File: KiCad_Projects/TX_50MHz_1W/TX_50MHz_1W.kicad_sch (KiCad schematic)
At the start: 3 parts, among them Q1 1W PA, U1 ESP32-S3, U2 Si5351A

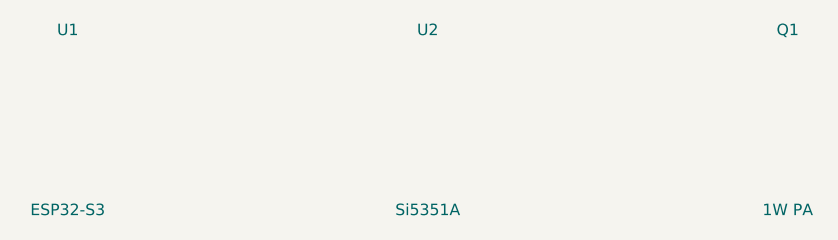
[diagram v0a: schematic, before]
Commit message: Add .kicad_pro project files for better compatibility with KiCad 8.0+
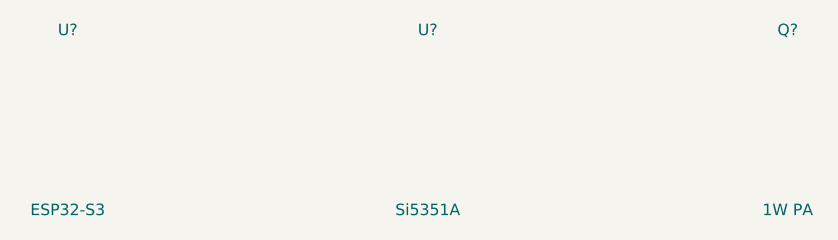
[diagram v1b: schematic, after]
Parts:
- renumbered Q1 to Q?, U1 to U?, U2 to U?
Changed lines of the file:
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@@
-(kicad_sch (version 20211123) (generator eeschema)
-  (paper "A4")
-  (symbol (lib_id "ESP32-S3-WROOM-1") (at 100 100 0) (unit 1)
-    (in_bom yes) (on_board yes) (fields_autoplaced)
-    (property "Reference" "U1" (id 0) (at 100 90 0))
-    (property "Value" "ESP32-S3" (id 1) (at 100 110 0))
-  )
-  (symbol (lib_id "RD01MUS2") (at 180 100 0) (unit 1)
-    (in_bom yes) (on_board yes) (fields_autoplaced)
-    (property "Reference" "Q1" (id 0) (at 180 90 0))
-    (property "Value" "1W PA" (id 1) (at 180 110 0))
-  )
-  (symbol (lib_id "Si5351A") (at 140 100 0) (unit 1)
-    (in_bom yes) (on_board yes) (fields_autoplaced)
-    (property "Reference" "U2" (id 0) (at 140 90 0))
-    (property "Value" "Si5351A" (id 1) (at 140 110 0))
-  )
-  (sheet_instances
-    (path "/" (page "1"))
-  )
+(kicad_sch
+	(version 20250114)
+	(generator "eeschema")
+	(generator_version "9.0")
+	(paper "A4")
+	(symbol
+		(lib_id "ESP32-S3-WROOM-1")
+		(at 100 100 0)
+		(unit 1)
+		(exclude_from_sim no)
+		(in_bom yes)
+		(on_board yes)
+		(dnp no)
+		(fields_autoplaced yes)
+		(property "Reference" "U?"
+			(at 100 90 0)
+			(effects
+				(font
+					(size 1.27 1.27)
+				)
+			)
+		)
+		(property "Value" "ESP32-S3"
+			(at 100 110 0)
+			(effects
+				(font
+					(size 1.27 1.27)
+				)
+			)
+		)
+		(property "Footprint" ""
+			(at 100 100 0)
+			(effects
+				(font
+					(size 1.27 1.27)
+				)
+			)
+		)
+		(property "Datasheet" ""
+			(at 100 100 0)
+			(effects
+				(font
+					(size 1.27 1.27)
+				)
+			)
+		)
+		(property "Description" ""
+			(at 100 100 0)
+			(effects
+				(font
+					(size 1.27 1.27)
+				)
+			)
+		)
+		(instances
+			(project "TX_50MHz_1W"
+				(path "/d09f74c9-7d1d-1ed1-03a7-fa9af5797810"
+					(reference "U?")
+					(unit 1)
+				)
+			)
+		)
+	)
+	(symbol
+		(lib_id "Si5351A")
+		(at 140 100 0)
+		(unit 1)
+		(exclude_from_sim no)
+		(in_bom yes)
+		(on_board yes)
+		(dnp no)
+		(fields_autoplaced yes)
+		(property "Reference" "U?"
+			(at 140 90 0)
+			(effects
+				(font
+					(size 1.27 1.27)
+				)
+			)
+		)
+		(property "Value" "Si5351A"
+			(at 140 110 0)
+			(effects
+				(font
+					(size 1.27 1.27)
+				)
+			)
+		)
+		(property "Footprint" ""
+			(at 140 100 0)
+			(effects
+				(font
+					(size 1.27 1.27)
+				)
+			)
+		)
+		(property "Datasheet" ""
+			(at 140 100 0)
+			(effects
+				(font
+					(size 1.27 1.27)
+				)
+			)
+		)
+		(property "Description" ""
+			(at 140 100 0)
+			(effects
+				(font
+					(size 1.27 1.27)
+				)
+			)
+		)
+		(instances
+			(project "TX_50MHz_1W"
+				(path "/d09f74c9-7d1d-1ed1-03a7-fa9af5797810"
+					(reference "U?")
+					(unit 1)
+				)
+			)
+		)
+	)
+	(symbol
+		(lib_id "RD01MUS2")
+		(at 180 100 0)
+		(unit 1)
+		(exclude_from_sim no)
+		(in_bom yes)
+		(on_board yes)
+		(dnp no)
+		(fields_autoplaced yes)
+		(property "Reference" "Q?"
+			(at 180 90 0)
+			(effects
+				(font
+					(size 1.27 1.27)
+				)
+			)
+		)
+		(property "Value" "1W PA"
+			(at 180 110 0)
+			(effects
+				(font
+					(size 1.27 1.27)
+				)
+			)
+		)
+		(property "Footprint" ""
+			(at 180 100 0)
+			(effects
+				(font
+					(size 1.27 1.27)
+				)
+			)
+		)
+		(property "Datasheet" ""
+			(at 180 100 0)
+			(effects
+				(font
+					(size 1.27 1.27)
+				)
+			)
+		)
+		(property "Description" ""
+			(at 180 100 0)
+			(effects
+				(font
+					(size 1.27 1.27)
+				)
+			)
+		)
+		(instances
+			(project "TX_50MHz_1W"
+				(path "/d09f74c9-7d1d-1ed1-03a7-fa9af5797810"
+					(reference "Q?")
+					(unit 1)
+				)
+			)
+		)
+	)
+	(sheet_instances
+		(path "/"
+			(page "1")
+		)
+	)
+	(embedded_fonts no)
 )

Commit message: Inject missing telemetry components into TX and RX schematic sheets
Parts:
- added FL?: 10.7MHz_Filter, symbol Kraft6M:10.7MHz_Filter
- added U?: SPF5043Z, symbol Kraft6M:SPF5043Z
- added U?: LT5560, symbol Kraft6M:LT5560
- added U?: BGS12PL6, symbol Kraft6M:BGS12PL6
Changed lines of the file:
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@@
 		)
 	)
-	(sheet_instances
+		(symbol
+		(lib_id "Kraft6M:BGS12PL6")
+		(at 200 150 0)
+		(unit 1)
+		(exclude_from_sim no)
+		(in_bom yes)
+		(on_board yes)
+		(dnp no)
+		(fields_autoplaced yes)
+		(property "Reference" "U?"
+			(at 200 140 0)
+			(effects (font (size 1.27 1.27)))
+		)
+		(property "Value" "BGS12PL6"
+			(at 200 160 0)
+			(effects (font (size 1.27 1.27)))
+		)
+		(property "Footprint" ""
+			(at 200 150 0)
+			(effects (font (size 1.27 1.27)) (hide yes))
+		)
+		(property "Datasheet" ""
+			(at 200 150 0)
+			(effects (font (size 1.27 1.27)) (hide yes))
+		)
+		(property "Description" ""
+			(at 200 150 0)
+			(effects (font (size 1.27 1.27)) (hide yes))
+		)
+		(instances
+			(project "TX_50MHz_1W"
+				(path "/d09f74c9-7d1d-1ed1-03a7-fa9af5797810"
+					(reference "U?")
+					(unit 1)
+				)
+			)
+		)
+	)
+	(symbol
+		(lib_id "Kraft6M:SPF5043Z")
+		(at 220 150 0)
+		(unit 1)
+		(exclude_from_sim no)
+		(in_bom yes)
+		(on_board yes)
+		(dnp no)
+		(fields_autoplaced yes)
+		(property "Reference" "U?"
+			(at 220 140 0)
+			(effects (font (size 1.27 1.27)))
+		)
+		(property "Value" "SPF5043Z"
+			(at 220 160 0)
+			(effects (font (size 1.27 1.27)))
+		)
+		(property "Footprint" ""
+			(at 220 150 0)
+			(effects (font (size 1.27 1.27)) (hide yes))
+		)
+		(property "Datasheet" ""
+			(at 220 150 0)
+			(effects (font (size 1.27 1.27)) (hide yes))
+		)
+		(property "Description" ""
+			(at 220 150 0)
+			(effects (font (size 1.27 1.27)) (hide yes))
+		)
+		(instances
+			(project "TX_50MHz_1W"
+				(path "/d09f74c9-7d1d-1ed1-03a7-fa9af5797810"
+					(reference "U?")
+					(unit 1)
+				)
+			)
+		)
+	)
+	(symbol
+		(lib_id "Kraft6M:LT5560")
+		(at 240 150 0)
+		(unit 1)
+		(exclude_from_sim no)
+		(in_bom yes)
+		(on_board yes)
+		(dnp no)
+		(fields_autoplaced yes)
+		(property "Reference" "U?"
+			(at 240 140 0)
+			(effects (font (size 1.27 1.27)))
+		)
+		(property "Value" "LT5560"
+			(at 240 160 0)
+			(effects (font (size 1.27 1.27)))
+		)
+		(property "Footprint" ""
+			(at 240 150 0)
+			(effects (font (size 1.27 1.27)) (hide yes))
+		)
+		(property "Datasheet" ""
+			(at 240 150 0)
+			(effects (font (size 1.27 1.27)) (hide yes))
+		)
+		(property "Description" ""
+			(at 240 150 0)
+			(effects (font (size 1.27 1.27)) (hide yes))
+		)
+		(instances
+			(project "TX_50MHz_1W"
+				(path "/d09f74c9-7d1d-1ed1-03a7-fa9af5797810"
+					(reference "U?")
+					(unit 1)
+				)
+			)
+		)
+	)
+	(symbol
+		(lib_id "Kraft6M:10.7MHz_Filter")
+		(at 260 150 0)
+		(unit 1)
+		(exclude_from_sim no)
+		(in_bom yes)
+		(on_board yes)
+		(dnp no)
+		(fields_autoplaced yes)
+		(property "Reference" "FL?"
+			(at 260 140 0)
+			(effects (font (size 1.27 1.27)))
+		)
+		(property "Value" "10.7MHz_Filter"
+			(at 260 160 0)
+			(effects (font (size 1.27 1.27)))
+		)
+		(property "Footprint" ""
+			(at 260 150 0)
+			(effects (font (size 1.27 1.27)) (hide yes))
+		)
+		(property "Datasheet" ""
+			(at 260 150 0)
+			(effects (font (size 1.27 1.27)) (hide yes))
+		)
+		(property "Description" ""
+			(at 260 150 0)
+			(effects (font (size 1.27 1.27)) (hide yes))
+		)
+		(instances
+			(project "TX_50MHz_1W"
+				(path "/d09f74c9-7d1d-1ed1-03a7-fa9af5797810"
+					(reference "FL?")
+					(unit 1)
+				)
+			)
+		)
+	)
+(sheet_instances
 		(path "/"
 			(page "1")
